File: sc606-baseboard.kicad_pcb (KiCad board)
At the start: 6 copper layers, 100 x 80 mm, 485 parts, among them IC1 TPS54561DPRT, IC2 TPS7A0518PDBVT, IC3 TPS7A0518PDBVT, IC4 AP22652W6-7, J1 1053131102, J10 E8124-015-01, J11 E8124-015-01, J12 E8124-015-01, J14 CONMMCX002-SMD-T, J2 WE_68715014522, J3 F52R-1A7H1-11020, J4 46756-1001, J5 U_FL-R-SMT-1_10_, J6 E8124-015-01, J7 DM3AT-SF-PEJM5, J8 693022010811, J9 E8124-015-01, M1 SC606T, Q1 BSS138APW, Q10 Si7223DN, Q11 Si7223DN, Q2 BSS138-7-F, Q3 BSS138APW, Q4 BSS138APW, Q5 BSS138APW, Q6 BSS138APW, Q7 BSS138-7-F, Q8 BSS138-7-F, Q9 SQS401EN-T1_BE3, SW1 1X03, U1 AP62301WU-7, U10 NCP163ASN330T1G, U11 EMIF06-MSD02N16, U12 STUSB4500QTR, U13 FT232RQ-REEL, U14 LTC4418IUF#PBF, U15 USB57442G, U2 AP62301WU-7, U3 AP62301WU-7, U4 74LVC1G123GN, U5 NTS0102GT, U6 PCA9547BS, U7 LT9611UXC, U8 NTS0102GT, U9 FSUSB30UMX, Y1 ABM8G-24.000MHZ-18-D2Y-T, Y2 ABM8G-25.000MHZ-B4Y-T

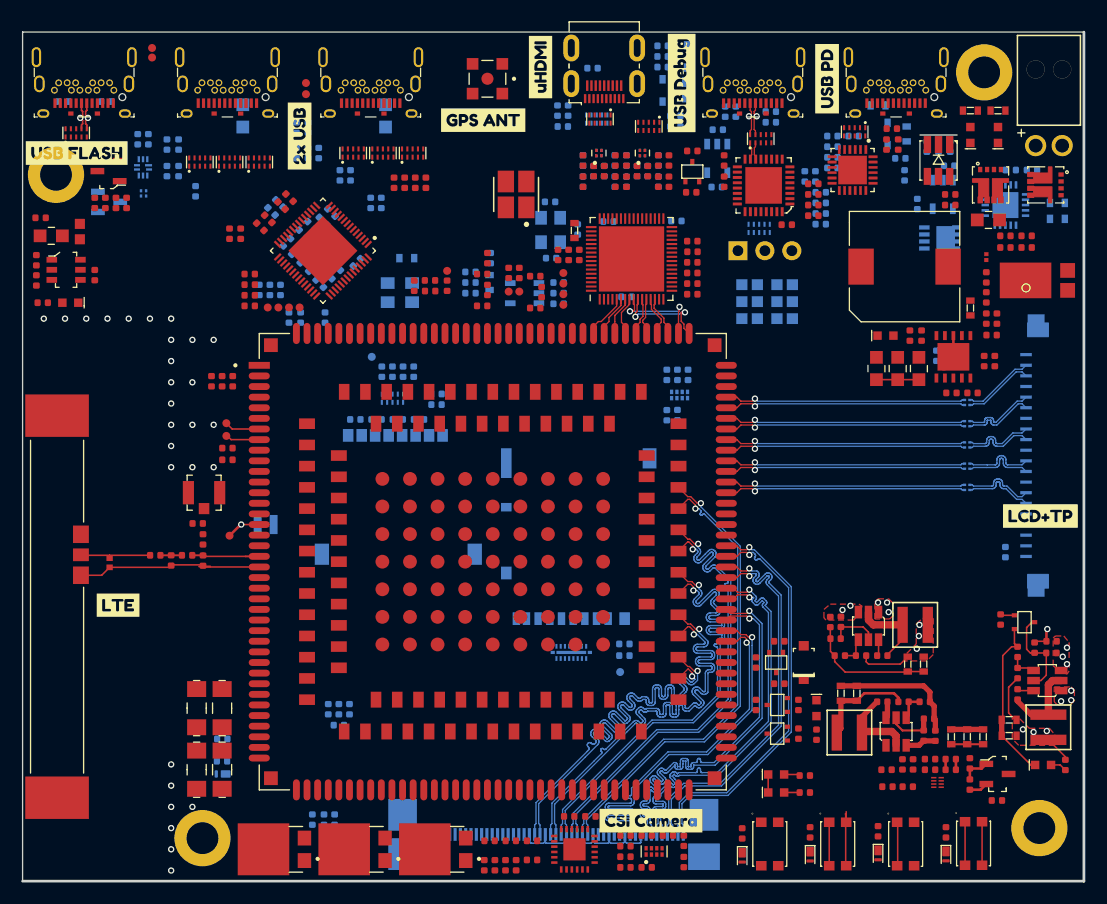
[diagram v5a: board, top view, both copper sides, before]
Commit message: Routed USB flash and both USB connectors differential signals with tuning
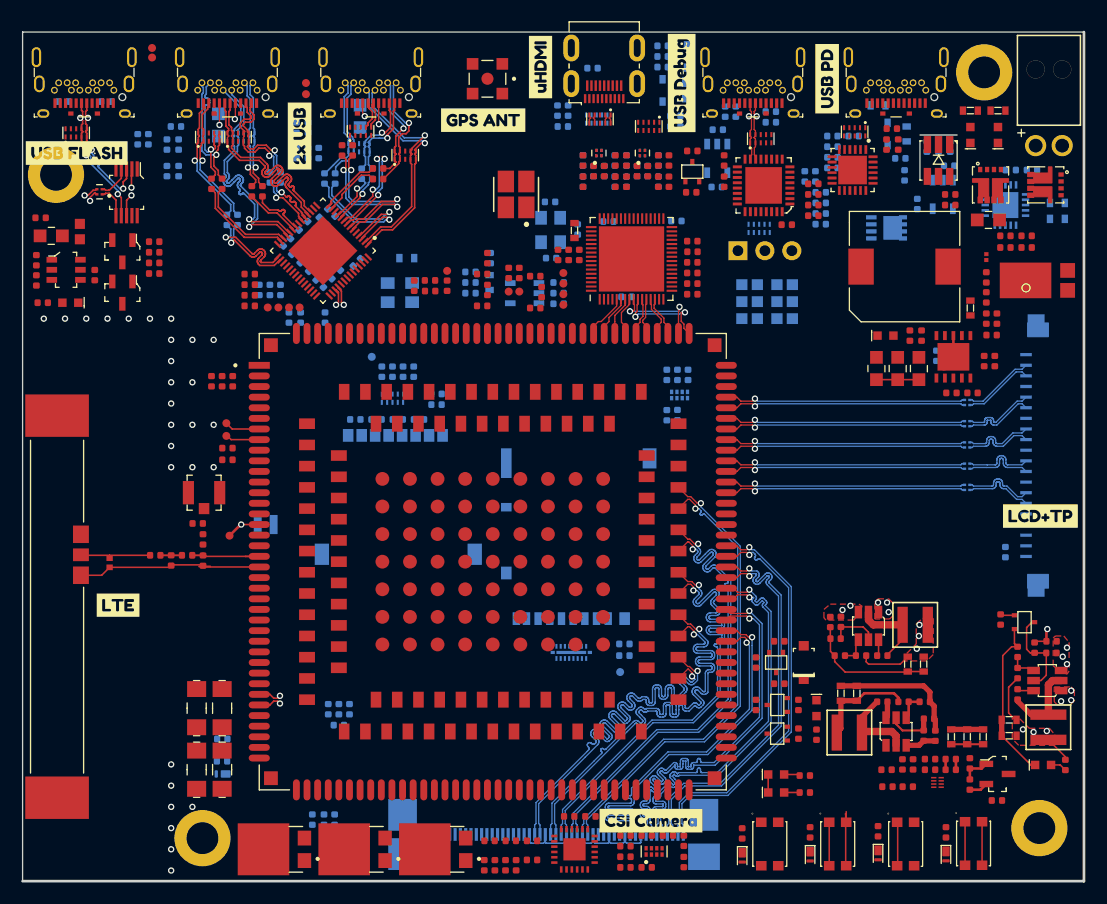
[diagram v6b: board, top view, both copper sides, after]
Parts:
- C102, C147, C149, C94, D25, D26, R134, R135: moved to B.Cu
- L22, Q8, R122, R124, R136, R137: moved to F.Cu
- Q9: footprint sc606-baseboard-footprints:Vishay_PowerPAK_1212-8_Single -> antmicro-footprints:Vishay_PowerPAK_1212-8_Single
- U9: value FSUSB30UMX -> FSUSB30MUX; footprint sc606-baseboard-footprints:UMLP-10_1.8x1.4mm -> antmicro-footprints:MSOP-10_W3mm; moved to F.Cu
- moved R111 8.69 mm to (88.0, 65.2), turned to 180 degrees
- moved Q8 8.64 mm to (85.0, 67.0), turned to 270 degrees
- moved Q7 7.66 mm to (85.0, 63.0), turned to 270 degrees
- moved R109 7.29 mm to (88.0, 64.2), turned to 180 degrees
- moved C151 6.37 mm to (90.0, 51.3), turned to 0 degrees
- moved C150 6.13 mm to (93.4, 56.7), turned to 270 degrees
- moved R110 5.88 mm to (88.0, 63.1), turned to 180 degrees
- moved C141 5.82 mm to (104.0, 56.2)
- moved C148 5.46 mm to (94.4, 56.7), turned to 270 degrees
- moved C102 5.12 mm to (107.5, 55.8)
- moved C94 5.12 mm to (108.5, 55.8)
- moved Q9 5.09 mm to (157.0, 60.9)
- moved R108 4.48 mm to (88.0, 62.1), turned to 0 degrees
- moved L22 4.15 mm to (82.8, 57.5), turned to 180 degrees
- moved C140 4.06 mm to (105.0, 56.2)
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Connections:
- D25 pad 1: /USB_HUB_Connectors/USB_C1_D1_N -> /USB_HUB_Connectors/USB_C1_SS_C_TX2_P
- D25 pad 10: /USB_HUB_Connectors/USB_C1_D1_N -> /USB_HUB_Connectors/USB_C1_SS_C_TX2_P
- D25 pad 2: /USB_HUB_Connectors/USB_C1_D1_P -> /USB_HUB_Connectors/USB_C1_SS_C_TX2_N
- D25 pad 4: /USB_HUB_Connectors/USB_C1_D2_N -> /USB_HUB_Connectors/USB_C1_SS_C_TX1_N
- D25 pad 5: /USB_HUB_Connectors/USB_C1_D2_P -> /USB_HUB_Connectors/USB_C1_SS_C_TX1_P
- D25 pad 6: /USB_HUB_Connectors/USB_C1_D2_P -> /USB_HUB_Connectors/USB_C1_SS_C_TX1_P
- D25 pad 7: /USB_HUB_Connectors/USB_C1_D2_N -> /USB_HUB_Connectors/USB_C1_SS_C_TX1_N
- D25 pad 9: /USB_HUB_Connectors/USB_C1_D1_P -> /USB_HUB_Connectors/USB_C1_SS_C_TX2_N
- D26 pad 1: /USB_HUB_Connectors/USB_C2_SS_C_RX1_N -> /USB_HUB_Connectors/USB_C2_D2_P
- D26 pad 10: /USB_HUB_Connectors/USB_C2_SS_C_RX1_N -> /USB_HUB_Connectors/USB_C2_D2_P
- D26 pad 2: /USB_HUB_Connectors/USB_C2_SS_C_RX1_P -> /USB_HUB_Connectors/USB_C2_D2_N
- D26 pad 4: /USB_HUB_Connectors/USB_C2_SS_C_TX1_N -> /USB_HUB_Connectors/USB_C2_SS_C_RX1_N
- D26 pad 5: /USB_HUB_Connectors/USB_C2_SS_C_TX1_P -> /USB_HUB_Connectors/USB_C2_SS_C_RX1_P
- D26 pad 6: /USB_HUB_Connectors/USB_C2_SS_C_TX1_P -> /USB_HUB_Connectors/USB_C2_SS_C_RX1_P
- D26 pad 7: /USB_HUB_Connectors/USB_C2_SS_C_TX1_N -> /USB_HUB_Connectors/USB_C2_SS_C_RX1_N
- D26 pad 9: /USB_HUB_Connectors/USB_C2_SS_C_RX1_P -> /USB_HUB_Connectors/USB_C2_D2_N
- D27 pad 4: /USB_HUB_Connectors/USB_C1_SS_C_TX2_N -> /USB_HUB_Connectors/USB_C1_D1_N
- D27 pad 5: /USB_HUB_Connectors/USB_C1_SS_C_TX2_P -> /USB_HUB_Connectors/USB_C1_D1_P
- D27 pad 6: /USB_HUB_Connectors/USB_C1_SS_C_TX2_P -> /USB_HUB_Connectors/USB_C1_D1_P
- D27 pad 7: /USB_HUB_Connectors/USB_C1_SS_C_TX2_N -> /USB_HUB_Connectors/USB_C1_D1_N
- D28 pad 4: /USB_HUB_Connectors/USB_C1_SS_C_TX1_N -> /USB_HUB_Connectors/USB_C1_D2_N
- D28 pad 5: /USB_HUB_Connectors/USB_C1_SS_C_TX1_P -> /USB_HUB_Connectors/USB_C1_D2_P
- D28 pad 6: /USB_HUB_Connectors/USB_C1_SS_C_TX1_P -> /USB_HUB_Connectors/USB_C1_D2_P
- D28 pad 7: /USB_HUB_Connectors/USB_C1_SS_C_TX1_N -> /USB_HUB_Connectors/USB_C1_D2_N
- D31 pad 1: /USB_HUB_Connectors/USB_C2_D2_P -> /USB_HUB_Connectors/USB_C2_D1_N
- D31 pad 10: /USB_HUB_Connectors/USB_C2_D2_P -> /USB_HUB_Connectors/USB_C2_D1_N
- D31 pad 2: /USB_HUB_Connectors/USB_C2_D2_N -> /USB_HUB_Connectors/USB_C2_D1_P
- D31 pad 4: /USB_HUB_Connectors/USB_C2_D1_N -> /USB_HUB_Connectors/USB_C2_SS_C_TX1_N
- D31 pad 5: /USB_HUB_Connectors/USB_C2_D1_P -> /USB_HUB_Connectors/USB_C2_SS_C_TX1_P
- D31 pad 6: /USB_HUB_Connectors/USB_C2_D1_P -> /USB_HUB_Connectors/USB_C2_SS_C_TX1_P
- D31 pad 7: /USB_HUB_Connectors/USB_C2_D1_N -> /USB_HUB_Connectors/USB_C2_SS_C_TX1_N
- D31 pad 9: /USB_HUB_Connectors/USB_C2_D2_N -> /USB_HUB_Connectors/USB_C2_D1_P
- U9 pad 1: USB_HUB_N -> /USB_flash_debug/USB_FLASH_ENABLE
- U9 pad 10: /USB_flash_debug/USB_FLASH_ENABLE -> 3V3_SYS
- U9 pad 2: /USB_flash_debug/USB_FLASH_P -> USB_HUB_N
- U9 pad 3: /USB_flash_debug/SoM_USB_Ferr_D_P -> /USB_flash_debug/USB_FLASH_P
- U9 pad 4: GND -> /USB_flash_debug/SoM_USB_Ferr_D_P
- U9 pad 5: /USB_flash_debug/SoM_USB_Ferr_D_N -> GND
- U9 pad 6: /USB_flash_debug/USB_FLASH_N -> /USB_flash_debug/SoM_USB_Ferr_D_N
- U9 pad 7: USB_HUB_P -> /USB_flash_debug/USB_FLASH_N
- U9 pad 8: Net-(R107-Pad1) -> USB_HUB_P
- U9 pad 9: 3V3_SYS -> Net-(R107-Pad1)
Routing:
- net SoM_USB_D_N: track 0.00 -> 63.8 mm, vias 0 -> 2
- net SoM_USB_D_P: track 0.00 -> 63.8 mm, vias 0 -> 2
- net USB_HUB_P: track 0.00 -> 28.7 mm, vias 0 -> 2
- net USB_HUB_N: track 0.00 -> 28.7 mm, vias 0 -> 2
- net /USB_HUB_Connectors/USB_C2_D2_P: track 0.00 -> 22.1 mm, vias 0 -> 1
- net /USB_HUB_Connectors/USB_C2_D2_N: track 0.00 -> 21.9 mm, vias 0 -> 1
- net /USB_HUB_Connectors/USB_C1_D2_P: track 0.00 -> 21.1 mm, vias 0 -> 1
- net /USB_HUB_Connectors/USB_C1_D2_N: track 0.00 -> 21.0 mm, vias 0 -> 1
- net /USB_HUB_Connectors/USB_C2_D1_P: track 0.00 -> 19.9 mm
- net /USB_HUB_Connectors/USB_C2_D1_N: track 0.00 -> 19.8 mm
- net /USB_HUB_Connectors/USB_C1_SS_RX2_P: track 0.00 -> 14.8 mm, vias 0 -> 2
- net /USB_HUB_Connectors/USB_C1_SS_RX2_N: track 0.00 -> 14.6 mm, vias 0 -> 2
- net /USB_HUB_Connectors/USB_C2_SS_C_RX2_N: track 0.00 -> 12.7 mm, vias 0 -> 1
- net /USB_HUB_Connectors/USB_C2_SS_C_TX2_P: track 0.00 -> 12.6 mm, vias 0 -> 1
- net /USB_HUB_Connectors/USB_C2_SS_C_RX2_P: track 0.00 -> 12.6 mm, vias 0 -> 1
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
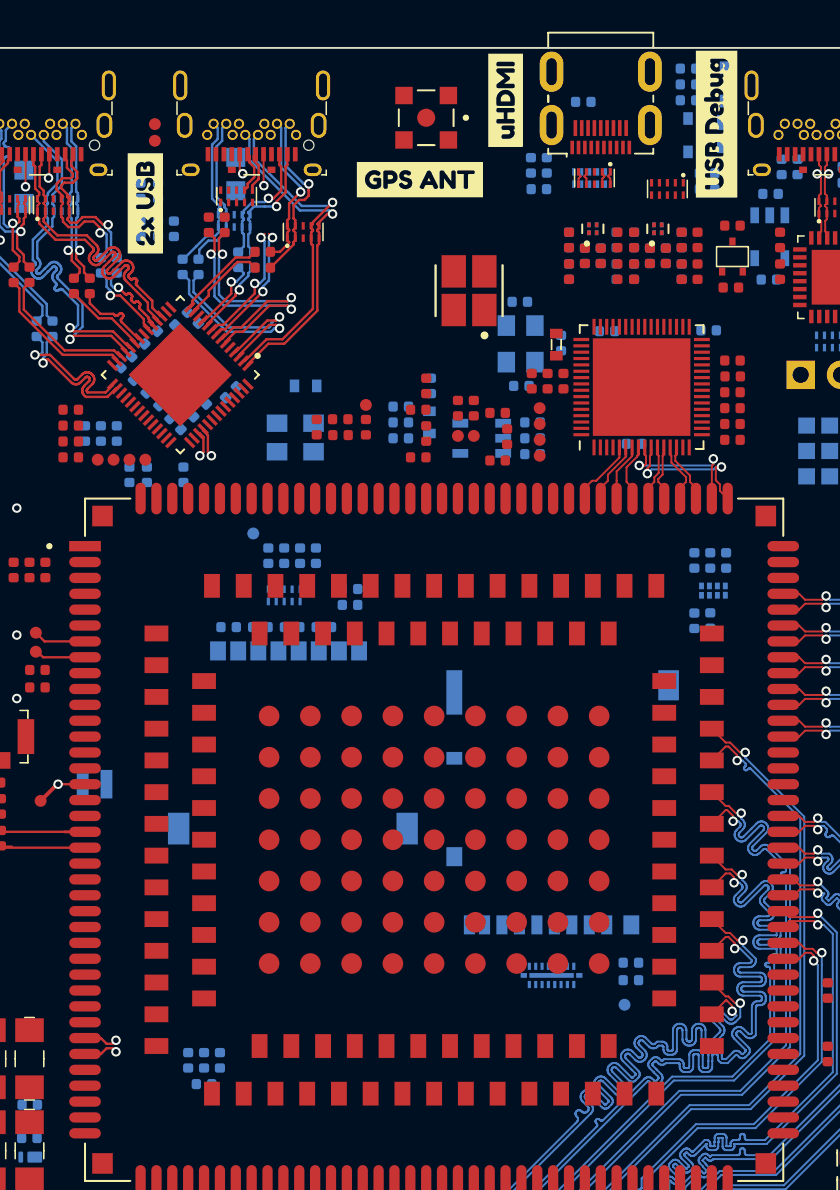
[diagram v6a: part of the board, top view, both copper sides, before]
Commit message: Finished routing differential pairs. Half of them already tuned
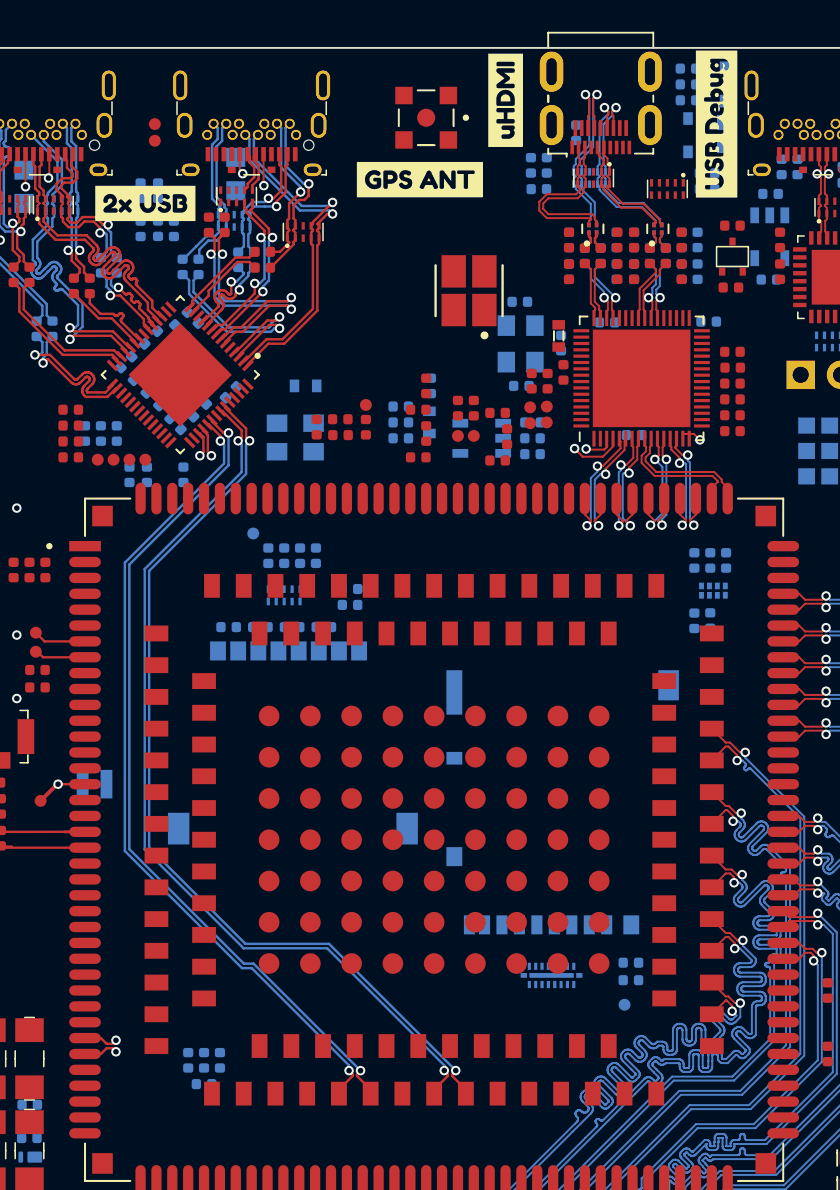
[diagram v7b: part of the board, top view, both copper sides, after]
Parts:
- C75, C76, R67, R68, R81, R82: moved to F.Cu
- C77, C78, C81, C82, R69, R70, R75, R76: moved to B.Cu
- moved TP5 2.15 mm to (127.0, 65.0)
- moved TP6 2.15 mm to (127.0, 66.0)
- moved R90 2.00 mm to (128.8, 47.8), turned to 270 degrees
- moved TP7 0.60 mm to (125.9, 65.0)
- moved TP8 0.60 mm to (125.9, 66.0)
- moved R58 0.57 mm to (127.8, 60.5)
- moved C49 0.55 mm to (137.2, 59.6)
- moved R53 0.55 mm to (138.7, 62.5)
- moved R57 0.55 mm to (138.7, 61.5)
- moved U7 0.55 mm to (132.8, 63.2)
- moved C47 0.55 mm to (130.3, 65.2)
- moved C48 0.55 mm to (133.3, 61.2)
- moved C50 0.55 mm to (130.8, 61.7)
- moved C51 0.55 mm to (132.3, 61.2)
- moved C52 0.55 mm to (133.8, 62.7)
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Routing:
- net SoM_USB3_TX_N: track 0.00 -> 58.1 mm, vias 0 -> 2
- net SoM_USB3_TX_P: track 0.00 -> 57.7 mm, vias 0 -> 2
- net SoM_USB3_RX_N: track 0.00 -> 52.5 mm, vias 0 -> 2
- net SoM_USB3_RX_P: track 0.00 -> 51.9 mm, vias 0 -> 2
- net /display module/TX_CLK_Ferr_P: track 0.00 -> 11.8 mm, vias 0 -> 1
- net /display module/TX_CLK_Ferr_N: track 0.00 -> 11.8 mm, vias 0 -> 1
- net /display module/TX_D1_Ferr_P: track 0.00 -> 11.5 mm, vias 0 -> 1
- net /display module/TX_D1_Ferr_N: track 0.00 -> 11.5 mm, vias 0 -> 1
- net /display module/TX_D2_Ferr_N: track 0.88 -> 10.3 mm
- net /display module/TX_D2_Ferr_P: track 0.88 -> 10.3 mm
- net /display module/TX_D0_Ferr_P: track 0.88 -> 7.41 mm
- net /display module/TX_D0_Ferr_N: track 0.88 -> 7.41 mm
- net SoMtoLT_D3_P: track 4.18 -> 8.86 mm, vias 0 -> 2
- net /display module/TX_D1_N: track 0.00 -> 4.57 mm, vias 0 -> 1
- net SoMtoLT_D2_P: track 3.99 -> 8.56 mm, vias 0 -> 2
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
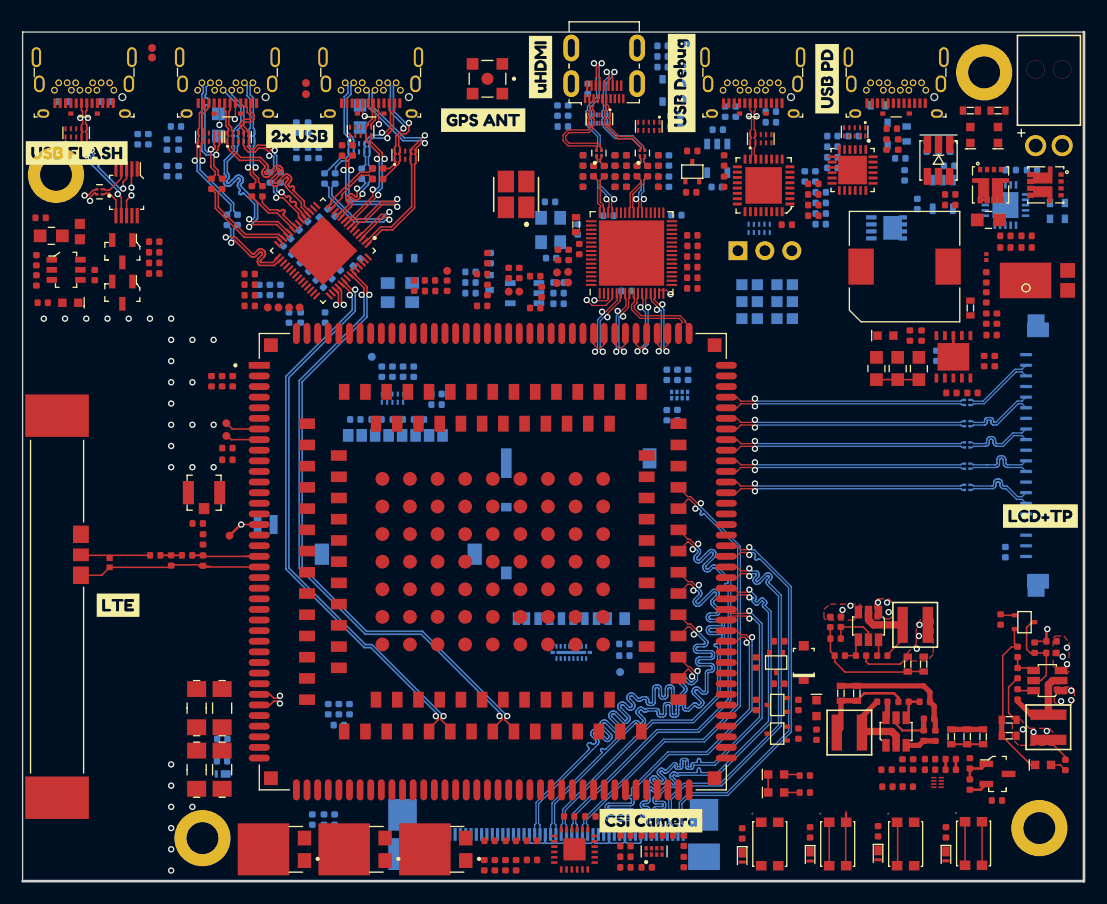
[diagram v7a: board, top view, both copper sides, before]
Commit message: Antenna signals routed
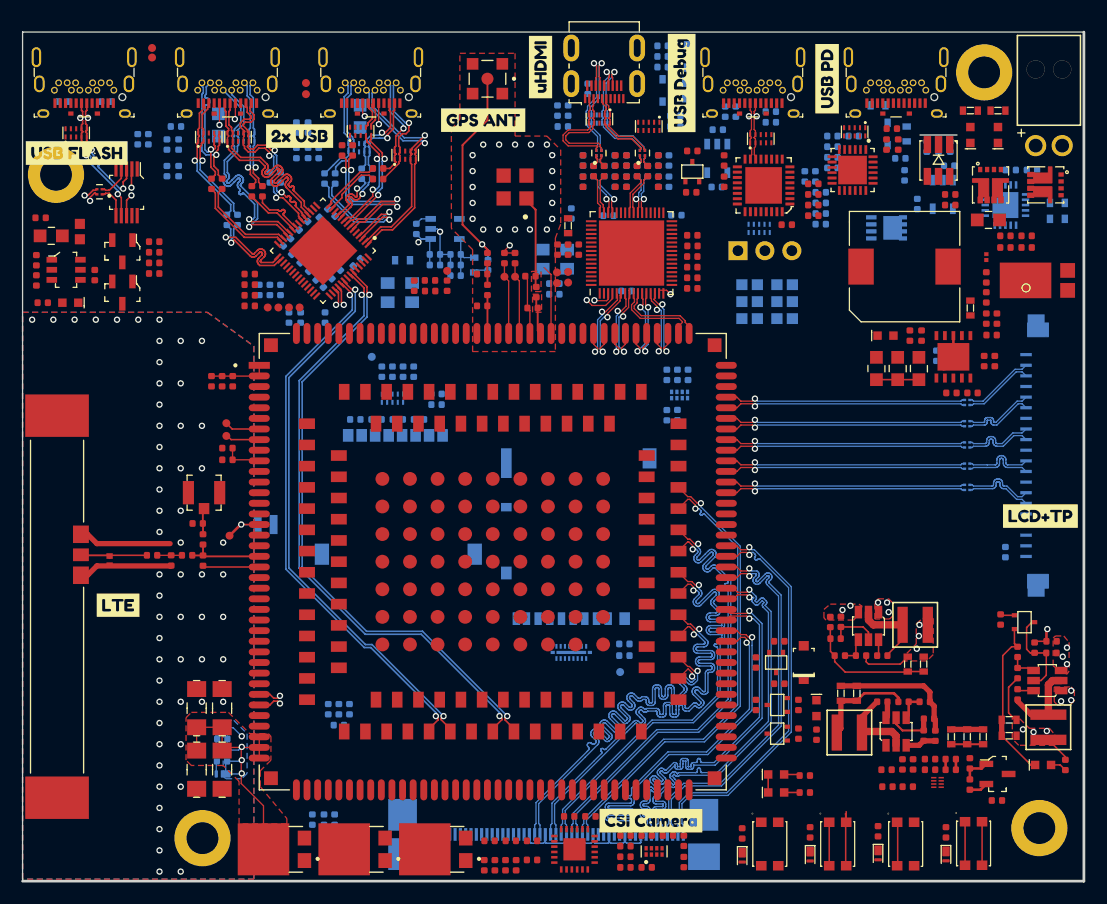
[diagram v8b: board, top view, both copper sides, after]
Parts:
- moved R92 15.1 mm to (112.7, 61.0), turned to 90 degrees
- moved C87 11.9 mm to (114.5, 64.3)
- moved C88 11.9 mm to (114.5, 63.4)
- moved U10 9.64 mm to (115.4, 61.0), turned to 90 degrees
- moved R52 5.55 mm to (125.7, 66.1), turned to 180 degrees
- moved C53 3.41 mm to (125.7, 67.1)
- moved Y1 2.68 mm to (125.8, 63.8), turned to 180 degrees
- moved C57 2.28 mm to (127.3, 59.5), turned to 90 degrees
- moved R94 2.20 mm to (118.2, 64.3), turned to 270 degrees
- moved C95 2.16 mm to (116.4, 65.3)
- moved C96 2.16 mm to (116.4, 64.3)
- moved C99 2.16 mm to (116.4, 63.4)
- moved R2 1.46 mm to (121.0, 63.7)
- moved R3 1.46 mm to (122.0, 63.7)
- moved TP3 1.46 mm to (122.0, 65.4)
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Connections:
- net Net-(C101-Pad1) renamed /peripherals/ANT_GNSS_
- net Net-(C90-Pad1) renamed /peripherals/ANT_LTE_UFL
- net Net-(C92-Pad1) renamed /peripherals/ANT_LTE
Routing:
- net V_SOM: track 0.00 -> 33.4 mm, vias 0 -> 4
- net GND: track 97.4 -> 127.2 mm, vias 29 -> 85
- net /peripherals/ANT_GNSS_: track 0.00 -> 20.1 mm, vias 0 -> 1
- net Net-(ANT1-Pad1): track 0.00 -> 8.61 mm
- net Net-(M1-Pad132): track 0.00 -> 6.78 mm
- net Net-(M1-Pad131): track 0.00 -> 6.78 mm
- net LDO6_1P8: track 0.00 -> 5.58 mm, vias 0 -> 1
- net Net-(C4-Pad1): track 0.00 -> 5.51 mm
- net 5V0_SYS: track 6.72 -> 12.0 mm, vias 5 -> 6
- net Net-(C95-Pad1): track 0.00 -> 4.90 mm
- net ANT_GNSS: track 0.00 -> 3.63 mm
- net ANT-WIFI: track 0.00 -> 3.58 mm
- net /peripherals/ANT_LTE_UFL: track 0.00 -> 2.47 mm
- net Net-(C101-Pad2): track 0.00 -> 2.04 mm
- net RTC_BAT: track 3.24 -> 4.79 mm
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- added copper zone on In1.Power_Plane, net 5V0_SYS
- added copper zone on F.Cu, net ANT-WIFI
- added copper zone on B.Cu, net GND
- added copper zone on In4.GND, net GND
- added copper zone on F.Cu, net Net-(ANT1-Pad1)
- added copper zone on B.Cu, net V_SOM
- added copper zone on F.Cu, net V_SOM
- removed copper zone on In1.Power_Plane, net GND
